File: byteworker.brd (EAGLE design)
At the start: 56 x 144.5 mm, 55 parts, among them IC1 MCP1703, IC2 TJA1043, J2 AVRSPI-61.27, Q1 BSS138, Q2 BSS138, Q3 BSS138, Q5 BSS138, Q6 FDN5618P, X1 16 MHz, X2 bus connector

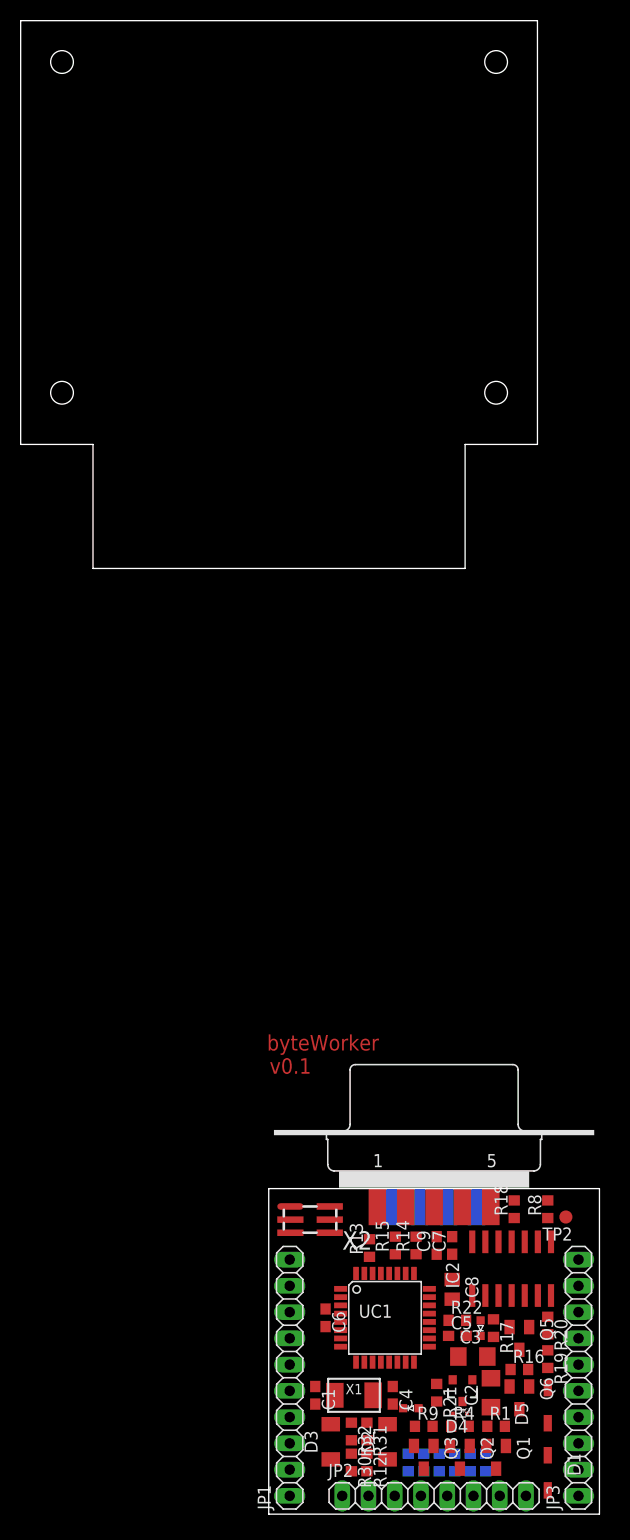
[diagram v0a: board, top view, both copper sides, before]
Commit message: - Shuffle some pins - Optional wake on input pins
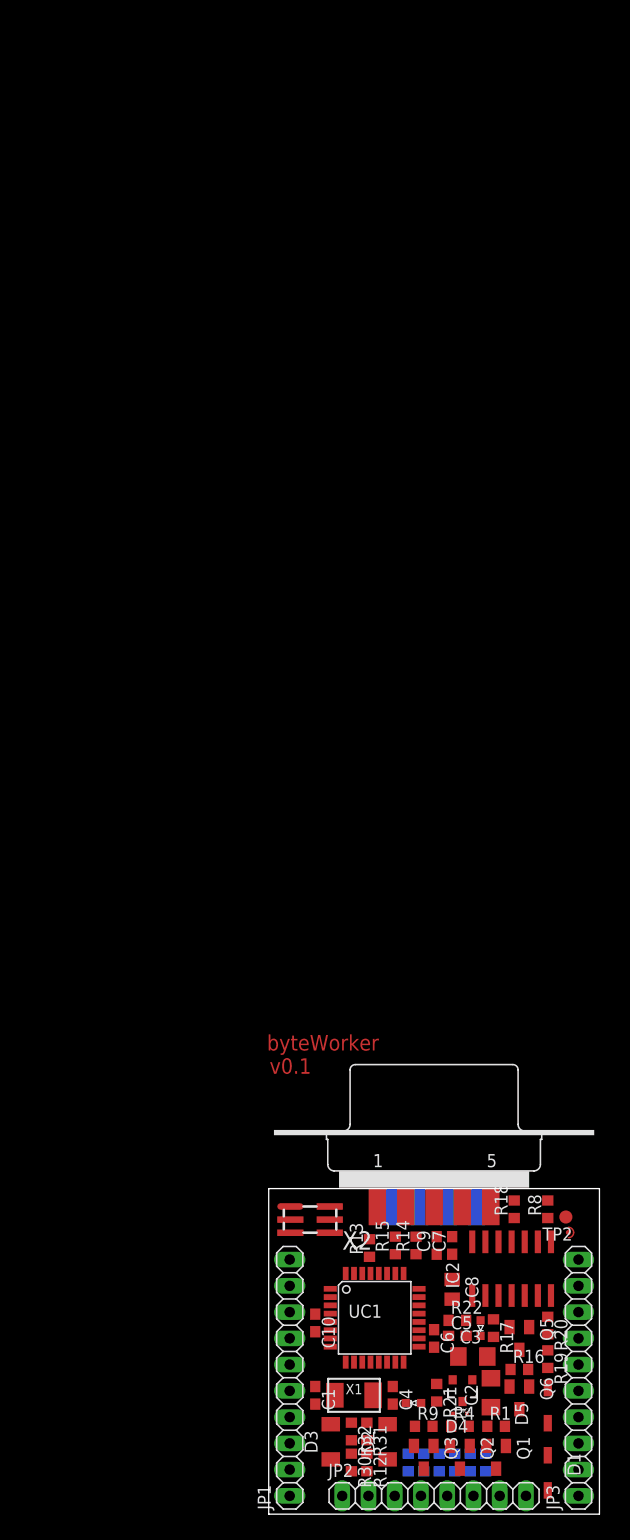
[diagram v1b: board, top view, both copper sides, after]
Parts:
- added C10: 100n, bytewerk-passive:C0603
- added JUMPER1: JUMPER-2_10, bytewerk-jumper:JMP2-1
- moved C6 10.7 mm to (0.00, 16.5)
- moved UC1 1.00 mm to (-5.75, 18.5)
- moved LED1 0.56 mm to (-2.00, 10.2)
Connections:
- removed net TESTLED3: UC1.29
- new net PD0: JP3.6, UC1.29
- net +5V: now also C10.1, JP2.4; no longer JP3.4
- net CANH: now also JP3.8; no longer JP3.9
- net CANL: now also JP3.7; no longer JP3.8
- net D2A: now also JP3.4; no longer JP3.6
- net GND: now also C10.2, JP3.10
- net IN0: now also JUMPER1.2
- net PD1: now also JP3.5; no longer JP3.7
- net VIN_BUS: no longer JP3.5
- net WAKE: now also JP3.9, JUMPER1.1; no longer JP3.10
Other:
- board size 56 x 144.5 mm -> 32 x 31.5 mm

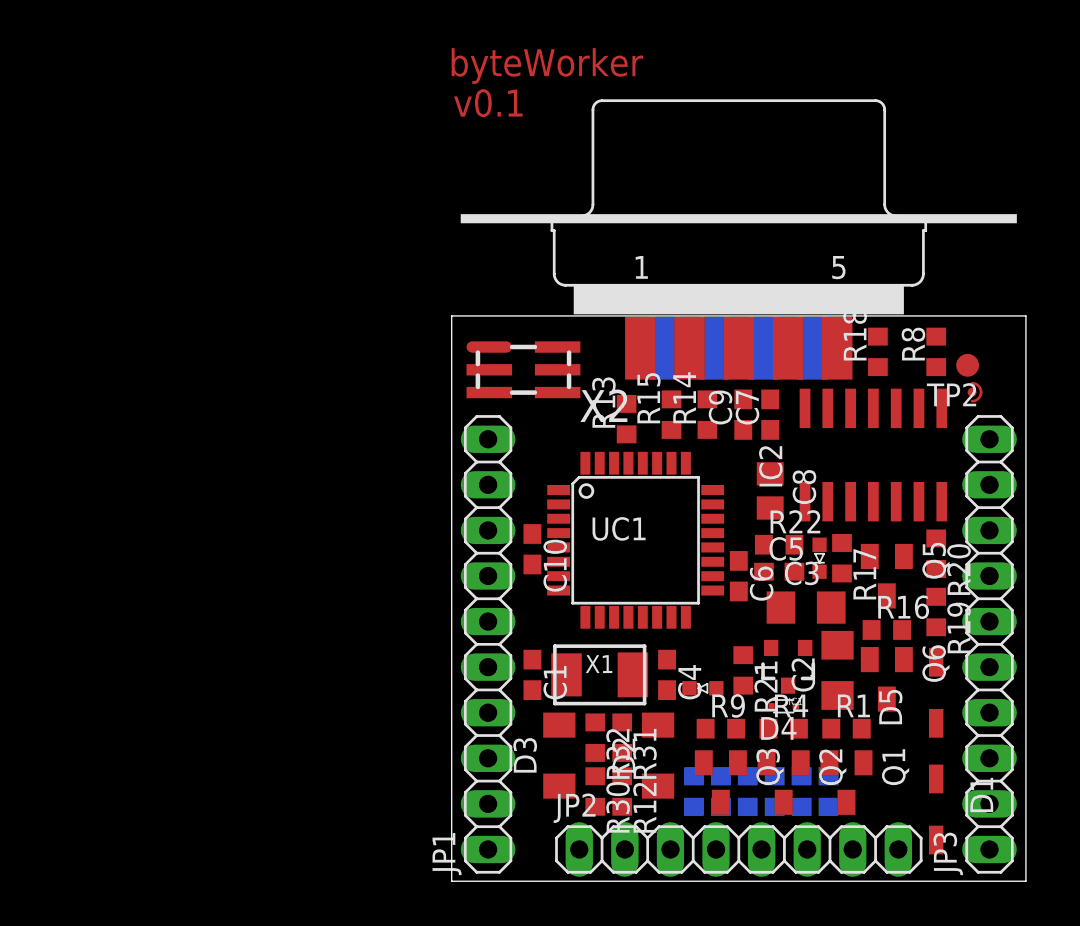
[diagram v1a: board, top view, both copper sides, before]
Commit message: - Some fixes in the schematics suggested by struppi - an incomplete board layout
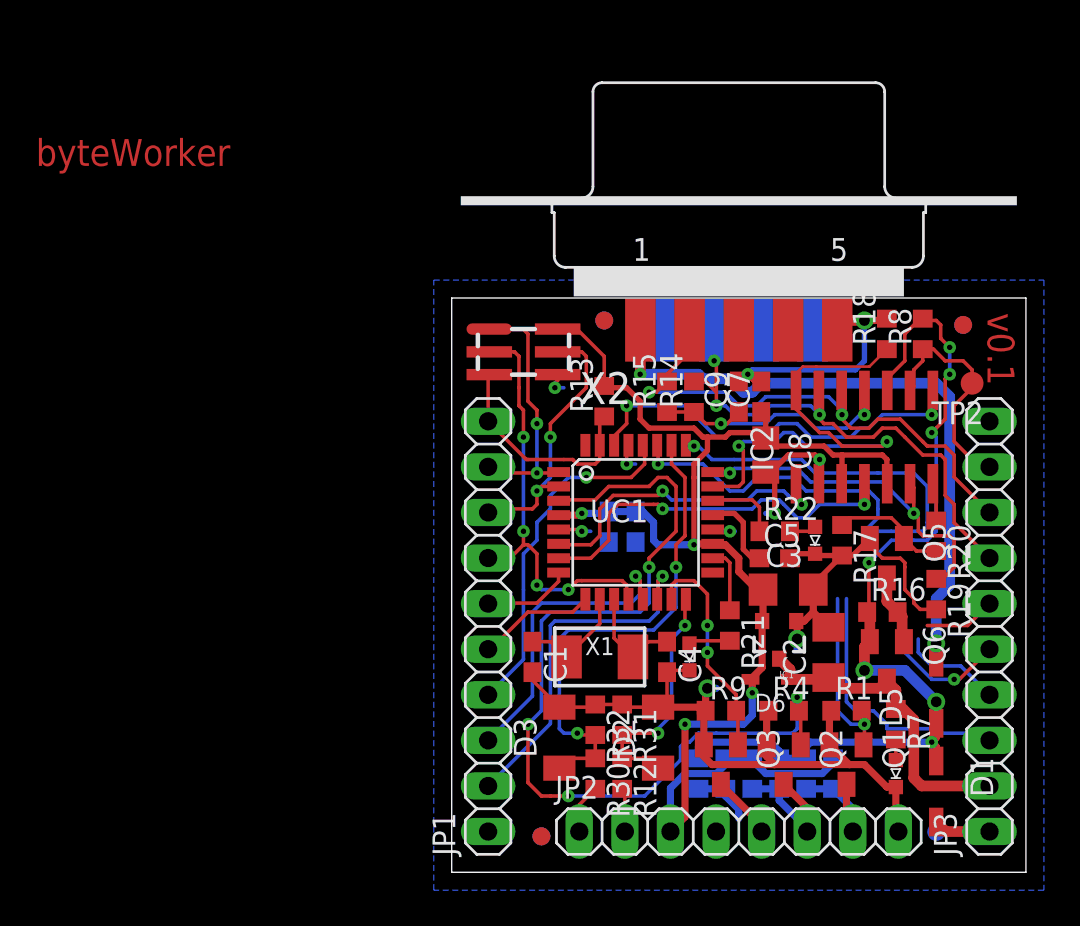
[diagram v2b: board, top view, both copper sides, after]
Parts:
- removed D4: SMS7630, bytewerk-passive:SC79_INFINEON
- removed JUMPER1: JUMPER-2_10, bytewerk-jumper:JMP2-1
- added D6: SCHOTTKY323, bytewerk-passive:SOD323
- added LED3: n.b.[red], bytewerk-led:LED0603
- added R7: n.b.[1k], bytewerk-passive:R0603
- added U$2, U$3, U$4, U$5, U$6, U$7, U$8: (no value), bytewerk-symbol:FIDUCIAL_R
- LED1: value red -> n.b.[yellow]
- LED2: value green -> n.b.[green]
- R15: value 62R -> n.b.[62R]
- R21, R22: value 1k -> n.b.[1k]
- moved C6 6.37 mm to (-5.75, 19.2), flipped to the bottom
- moved C10 4.43 mm to (-7.25, 19.2), flipped to the bottom
- moved R21 2.61 mm to (-0.50, 13.8)
- moved C8 2.02 mm to (1.50, 23.2)
- moved LED1 1.90 mm to (-2.75, 12.0), turned to 270 degrees
- moved R13 1.60 mm to (-7.50, 26.2)
- moved IC1 1.58 mm to (2.25, 13.0)
- moved C3 1.41 mm to (2.75, 15.8)
- moved R14 1.25 mm to (-2.50, 26.5)
- moved R8 1.25 mm to (10.2, 30.0)
- moved C2 1.12 mm to (5.00, 12.2)
- moved C7 1.12 mm to (1.25, 26.5)
- moved IC2 1.12 mm to (7.00, 24.2)
- moved R18 1.12 mm to (8.25, 30.0)
- moved C9 1.03 mm to (0.00, 26.5)
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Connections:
- new net N$8: LED3.A, R7.2
- net +5V: now also D6.A, JP2.3; no longer D4.A, JP2.4
- net CANH: now also JP3.7; no longer JP3.8
- net CANL: now also JP3.8; no longer JP3.7
- net GND: now also LED3.C
- net IN0: no longer JUMPER1.2
- net VOUT_SW: now also D6.C, R7.1; no longer D4.C
- net WAKE: no longer JUMPER1.1
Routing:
- net GND: track 0.00 -> 85.9 mm, vias 0 -> 9
- net +5V: track 0.00 -> 80.1 mm, vias 0 -> 4
- net VIN_RECT: track 0.00 -> 52.9 mm, vias 0 -> 7
- net SS_A/OC1B: track 0.00 -> 51.9 mm, vias 0 -> 4
- net VIN_BUS: track 0.00 -> 35.8 mm, vias 0 -> 2
- net CANL: track 0.00 -> 29.6 mm, vias 0 -> 2
- net CANH: track 0.00 -> 29.0 mm, vias 0 -> 3
- net UC_IN1: track 0.00 -> 27.5 mm, vias 0 -> 2
- net PB6: track 0.00 -> 26.9 mm, vias 0 -> 2
- net !CAN_STB!: track 0.00 -> 26.5 mm, vias 0 -> 2
- net D2A: track 0.00 -> 25.9 mm, vias 0 -> 1
- net RXD/SCK_A: track 0.00 -> 23.6 mm, vias 0 -> 4
- net !CAN_ERR!: track 0.00 -> 22.7 mm, vias 0 -> 2
- net CAN_RX: track 0.00 -> 21.3 mm, vias 0 -> 2
- net CAN_EN: track 0.00 -> 20.2 mm, vias 0 -> 2
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- added copper zone on layer 16, net GND
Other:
- board size 32 x 31.5 mm -> 32 x 32 mm
- board text removed: "PASSMARKER"

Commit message: Layout finish
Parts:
- moved C10 0.35 mm to (-7.50, 19.0)
- moved C6 0.35 mm to (-6.00, 19.5)
- moved LED2 0.25 mm to (4.25, 18.8)
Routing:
- net PD1: track 6.04 -> 45.5 mm, vias 1 -> 2
- net PD0: track 5.56 -> 40.5 mm, vias 1 -> 2
- net PB6: track 26.9 -> 41.4 mm
- net PC4: track 14.8 -> 25.3 mm, vias 0 -> 1
- net D2A: track 25.9 -> 34.3 mm
- net GND: track 85.9 -> 89.4 mm, vias 9 -> 10
- net PD6/ADC3: track 20.2 -> 17.6 mm
- net PB7/SCK: track 19.6 -> 21.4 mm
- net PD7: track 12.3 -> 10.7 mm
- net !CAN_ERR!: track 22.7 -> 21.5 mm
- net CANL: track 29.6 -> 30.6 mm
- net OUT2: track 7.52 -> 8.31 mm
- net !RESET!: track 12.4 -> 13.1 mm
- net PD5/ADC2: track 17.1 -> 16.6 mm
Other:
- board text added: "byte- Worker"
- board text removed: "byteWorker"

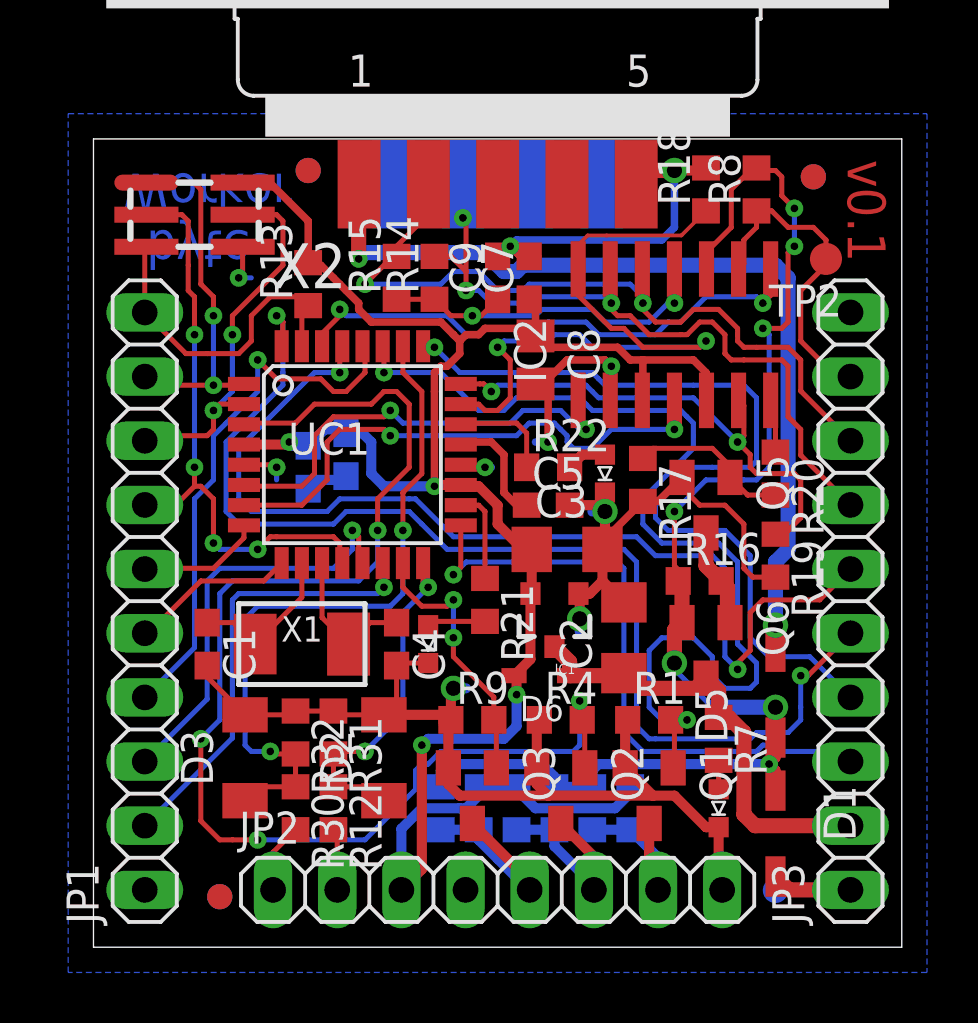
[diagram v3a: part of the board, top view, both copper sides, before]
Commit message: v0.2: - Changed resistor values - Re-aligned pinheaders
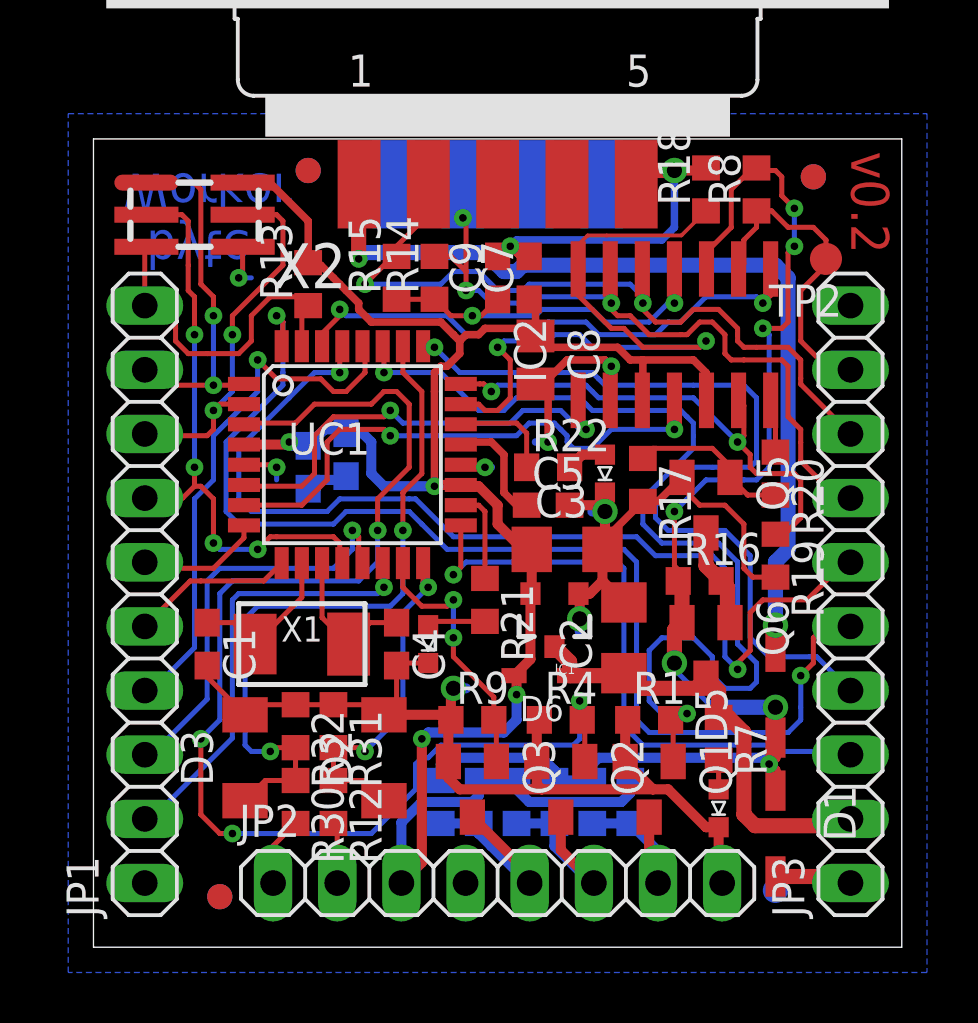
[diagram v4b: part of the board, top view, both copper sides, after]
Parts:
- R10, R2, R5: value 10k -> 1k
- R21, R22: value n.b.[1k] -> 1k
- moved JP1 0.27 mm to (-14.0, 14.0)
- moved JP3 0.27 mm to (14.0, 14.0)
- moved JP2 0.27 mm to (0.00, 2.54)
- moved Q1 0.25 mm to (6.00, 6.25)
- moved Q2 0.25 mm to (2.50, 6.25)
- moved Q3 0.25 mm to (-1.00, 6.25)
- moved R10 0.25 mm to (-0.75, 5.75)
- moved R11 0.25 mm to (-2.25, 5.75)
- moved R12 0.25 mm to (-6.50, 5.75)
- moved R2 0.25 mm to (5.25, 5.75)
- moved R3 0.25 mm to (3.75, 5.75)
- moved R30 0.25 mm to (-8.00, 5.75)
- moved R31 0.25 mm to (-6.50, 8.75)
- moved R32 0.25 mm to (-8.00, 8.75)
- moved R5 0.25 mm to (0.75, 5.75)
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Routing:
- net GND: track 89.4 -> 88.6 mm
- net SS_A/OC1B: track 51.9 -> 51.3 mm
- net !RESET!: track 13.1 -> 13.7 mm
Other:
- board text added: "v0.2"
- board text removed: "v0.1"
